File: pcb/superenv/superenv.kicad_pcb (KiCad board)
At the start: 2 copper layers, 100 x 100 mm, 25 parts, among them J1 TYPE-C-31-M-04, J2 Power-Header, J3 UART, J4 I2C, J5 I2C, U1 ESP32-C6-WROOM-1, U2 AMS1117-3.3, U3 DS18B20, U4 DS18B20, U5 DS18B20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

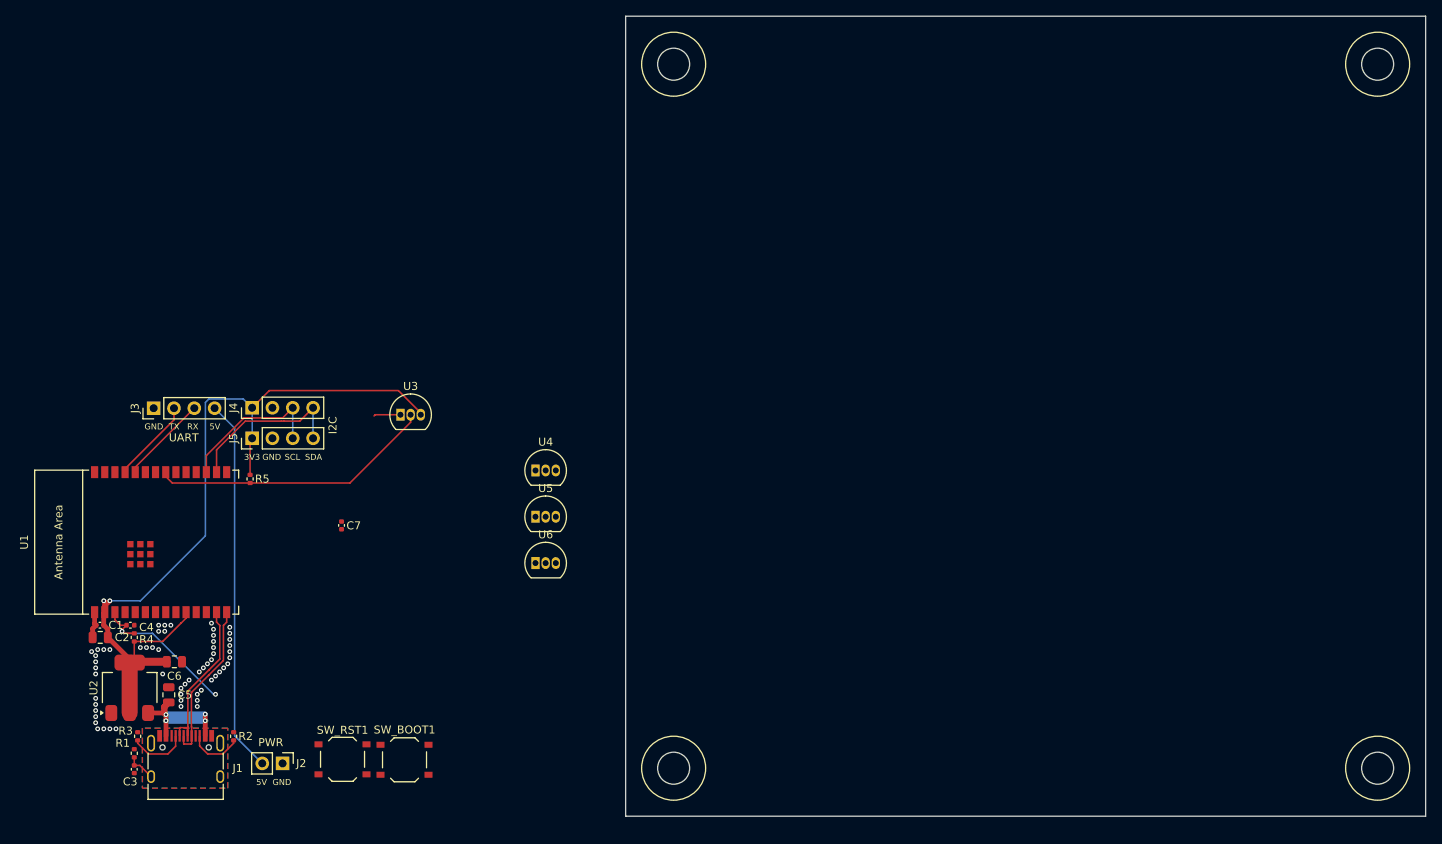
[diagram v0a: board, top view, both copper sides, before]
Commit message: Add I2C sensors
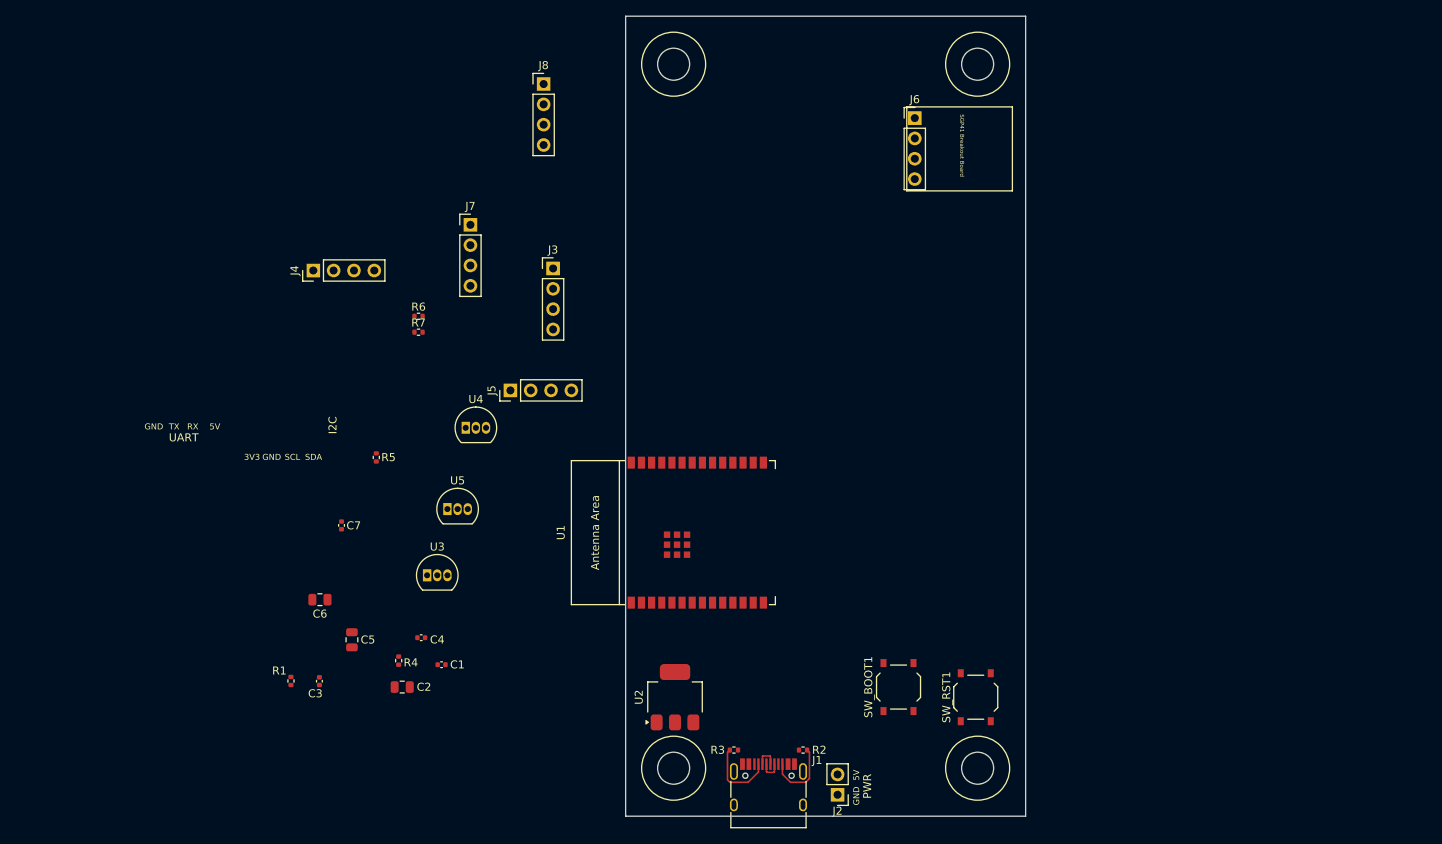
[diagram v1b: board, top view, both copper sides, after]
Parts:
- removed U6: DS18B20, Package_TO_SOT_THT:TO-92_Inline
- added J6: SGP41BB, Connector_PinHeader_2.54mm:PinHeader_1x04_P2.54mm_Vertical, F.Cu at (136.1, 62.7)
- added J7: SCD41BB, Connector_PinHeader_2.54mm:PinHeader_1x04_P2.54mm_Vertical, F.Cu at (80.6, 76.1)
- added J8: AHT20+BMP280BB, Connector_PinHeader_2.54mm:PinHeader_1x04_P2.54mm_Vertical, F.Cu at (89.8, 58.5)
- added R6: 4.7k, Resistor_SMD:R_0402_1005Metric, F.Cu at (74.1, 87.5)
- added R7: 4.7k, Resistor_SMD:R_0402_1005Metric, F.Cu at (74.1, 89.5)
- moved SW_RST1 79.5 mm to (143.8, 135.1), turned to -90 degrees
- moved R3 74.6 mm to (113.5, 141.7), turned to 0 degrees
- moved J1 72.9 mm to (117.9, 147.5)
- moved R2 71.2 mm to (122.2, 141.7), turned to 180 degrees
- moved J2 69.5 mm to (126.5, 147.3), turned to 180 degrees
- moved U2 68.2 mm to (106.2, 135.1)
- moved U1 67.1 mm to (109.0, 114.6)
- moved SW_BOOT1 62.4 mm to (134.1, 133.9), turned to 90 degrees
- moved J3 52.9 mm to (90.9, 81.5), turned to 0 degrees
- moved C1 43.0 mm to (77.0, 131.1)
- moved C2 38.3 mm to (72.1, 133.9)
- moved C4 36.4 mm to (74.5, 127.7)
- moved R4 33.2 mm to (71.6, 130.6)
- moved J5 32.8 mm to (85.6, 96.8)
- moved C3 25.6 mm to (61.7, 133.1)
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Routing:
- net +3V3: track 103.0 -> 0.00 mm, vias 2 -> 0
- net +5V: track 65.9 -> 0.00 mm, vias 4 -> 0
- net DQ: track 35.6 -> 0.00 mm
- net SDA: track 20.8 -> 0.00 mm
- net EN: track 20.3 -> 0.00 mm, vias 2 -> 0
- net SCL: track 19.2 -> 0.00 mm
- net USB_DN: track 20.3 -> 2.99 mm
- net USB_DP: track 20.3 -> 2.99 mm
- net RXD_0: track 11.1 -> 0.00 mm
- net TXD_0: track 10.5 -> 0.00 mm
- net GND: track 6.78 -> 0.00 mm, vias 58 -> 0
- net Net-(J1-SHIELD): track 3.69 -> 0.00 mm
- net Net-(J1-CC2): track 6.84 -> 8.92 mm
- net Net-(J1-CC1): track 7.36 -> 9.36 mm
- removed copper zone on B.Cu, net Net-(J1-SHIELD)
- removed copper zone on F.Cu, net Net-(J1-SHIELD)
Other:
- board size 100 x 100 mm -> 50 x 100 mm
- board text added: "SGP41 Breakout Board"

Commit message: Add stuff
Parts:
- added J10: PMSBB, Connector_JST:JST_GH_BM08B-GHS-TBT_1x08-1MP_P1.25mm_Vertical, F.Cu at (145.5, 108.1)
- added J9: UART1, Connector_PinHeader_2.54mm:PinHeader_1x04_P2.54mm_Vertical, F.Cu at (130.8, 118.9)
- J3: value UART -> UART0
- moved J7 77.6 mm to (145.8, 118.1), turned to -90 degrees
- moved J4 66.5 mm to (123.2, 105.2)
- moved R7 65.3 mm to (135.4, 112.0), turned to 90 degrees
- moved R6 64.3 mm to (133.6, 112.0), turned to 90 degrees
- moved C7 57.0 mm to (120.7, 123.5)
- moved R1 55.8 mm to (112.0, 147.6)
- moved J3 51.8 mm to (130.8, 114.6), turned to -90 degrees
- moved C3 51.3 mm to (111.0, 147.5), turned to -90 degrees
- moved C5 46.6 mm to (111.0, 139.1), turned to -90 degrees
- moved C6 45.7 mm to (107.0, 129.3)
- moved R5 41.7 mm to (110.5, 102.9), turned to 180 degrees
- moved J5 39.7 mm to (123.2, 109.5)
- moved R4 34.4 mm to (105.9, 127.3)
- moved C4 32.0 mm to (106.4, 125.2)
- moved C2 30.7 mm to (102.0, 127.0)
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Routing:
- net +3V3: track 0.00 -> 108.6 mm, vias 0 -> 1
- net +5V: track 0.00 -> 59.4 mm, vias 0 -> 4
- net SCL: track 0.00 -> 57.7 mm
- net SDA: track 0.00 -> 49.5 mm
- net BOOT: track 0.00 -> 38.0 mm, vias 0 -> 2
- net TXD_1: track 0.00 -> 30.6 mm
- net EN: track 0.00 -> 29.8 mm, vias 0 -> 2
- net TXD_0: track 0.00 -> 29.4 mm
- net RXD_1: track 0.00 -> 29.3 mm
- net RXD_0: track 0.00 -> 25.6 mm
- net USB_DP: track 2.99 -> 24.7 mm
- net USB_DN: track 2.99 -> 24.7 mm
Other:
- board text added: "SCD41 Breakout Board"

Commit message: Update gitignore and finish v1
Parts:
- removed the C3 at (111.0, 147.5)
- removed U5: DS18B20, Package_TO_SOT_THT:TO-92_Inline
- added C4: 100n, Capacitor_SMD:C_0603_1608Metric, F.Cu at (121.9, 123.4)
- added G***: LOGO, LOGO, B.Cu at (142.4, 119.5)
- added J11: DS18B20, Connector_PinHeader_2.54mm:PinHeader_1x03_P2.54mm_Vertical, F.Cu at (130.0, 139.2)
- added J12: GPIO, Connector_PinHeader_2.54mm:PinHeader_1x08_P2.54mm_Vertical, F.Cu at (110.0, 83.3)
- added J13: 3V3 rail, Connector_PinHeader_2.54mm:PinHeader_1x04_P2.54mm_Vertical, F.Cu at (101.9, 93.5)
- added J14: GND rail, Connector_PinHeader_2.54mm:PinHeader_1x04_P2.54mm_Vertical, F.Cu at (105.5, 93.5)
- added R8: 10k, Resistor_SMD:R_0603_1608Metric, F.Cu at (135.8, 131.6)
- added R9: 10k, Resistor_SMD:R_0603_1608Metric, F.Cu at (135.7, 130.0)
- C1: footprint Capacitor_SMD:C_0402_1005Metric -> Capacitor_SMD:C_0603_1608Metric
- C3: renamed from C4; footprint Capacitor_SMD:C_0402_1005Metric -> Capacitor_SMD:C_0603_1608Metric
- C7: value 100n -> 4.7n; footprint Capacitor_SMD:C_0402_1005Metric -> Capacitor_SMD:C_0603_1608Metric
- R1, R2, R3, R4, R5, R6, R7: footprint Resistor_SMD:R_0402_1005Metric -> Resistor_SMD:R_0603_1608Metric
- moved J8 54.4 mm to (134.5, 89.4)
- moved U3 54.1 mm to (130.0, 126.2), turned to -90 degrees
- moved U4 33.9 mm to (113.5, 96.3)
- moved J10 32.8 mm to (136.6, 139.7)
- moved C7 26.8 mm to (109.0, 147.6)
- moved J7 14.5 mm to (145.0, 103.6)
- moved J6 9.01 mm to (130.1, 96.8), turned to 180 degrees
- moved R5 7.54 mm to (117.9, 101.6)
- moved R3 2.99 mm to (111.0, 143.3), turned to 90 degrees
- moved R2 2.82 mm to (124.5, 143.3), turned to 90 degrees
- moved R7 1.65 mm to (136.1, 110.6), turned to -90 degrees
- moved R6 1.55 mm to (134.1, 110.6), turned to -90 degrees
- moved J2 1.26 mm to (127.5, 147.3)
- moved R1 1.02 mm to (111.0, 147.5)
- moved C3 0.60 mm to (106.9, 125.0)
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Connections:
- C7 pad 1: BOOT -> Net-(J1-SHIELD)
- J10 pad 1: unconnected-(J10-Pin_1-Pad1) -> +5V
- J10 pad 2: unconnected-(J10-Pin_2-Pad2) -> GND
- J10 pad 3: unconnected-(J10-Pin_3-Pad3) -> SET
- J10 pad 4: unconnected-(J10-Pin_4-Pad4) -> TXD_0
- J10 pad 5: unconnected-(J10-Pin_5-Pad5) -> RXD_0
- J10 pad 6: unconnected-(J10-Pin_6-Pad6) -> RST
- R6 pad 1: +3V3 -> SCL
- R6 pad 2: SCL -> +3V3
- R7 pad 1: +3V3 -> SDA
- R7 pad 2: SDA -> +3V3
- U1 pad 11: unconnected-(U1-GPIO10-Pad11) -> SET
- U1 pad 12: unconnected-(U1-GPIO11-Pad12) -> RST
- U1 pad 18: unconnected-(U1-GPIO20-Pad18) -> GPIO20
- U1 pad 19: unconnected-(U1-GPIO21-Pad19) -> GPIO21
- U1 pad 20: unconnected-(U1-GPIO22-Pad20) -> GPIO22
- U1 pad 4: unconnected-(U1-MTMS/GPIO4/ADC1_CH4-Pad4) -> GPIO4
- U1 pad 5: unconnected-(U1-MTDI/GPIO5/ADC1_CH5-Pad5) -> GPIO5
- U1 pad 6: unconnected-(U1-MTCK/GPIO6/ADC1_CH6-Pad6) -> GPIO6
- U1 pad 7: unconnected-(U1-MTDO/GPIO7-Pad7) -> GPIO7
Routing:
- net +3V3: track 108.6 -> 210.7 mm
- net DQ: track 0.00 -> 65.4 mm, vias 0 -> 1
- net RST: track 0.00 -> 48.4 mm, vias 0 -> 2
- net SET: track 0.00 -> 42.5 mm, vias 0 -> 2
- net GPIO4: track 0.00 -> 38.8 mm, vias 0 -> 1
- net GPIO5: track 0.00 -> 35.7 mm, vias 0 -> 1
- net GPIO6: track 0.00 -> 32.7 mm, vias 0 -> 1
- net RXD_0: track 25.6 -> 56.8 mm, vias 0 -> 1
- net GPIO7: track 0.00 -> 29.6 mm, vias 0 -> 1
- net TXD_0: track 29.4 -> 57.4 mm, vias 0 -> 1
- net +5V: track 59.4 -> 81.5 mm
- net GPIO20: track 0.00 -> 10.6 mm
- net GPIO21: track 0.00 -> 7.54 mm
- net GPIO22: track 0.00 -> 4.48 mm
- net SDA: track 49.5 -> 53.3 mm
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- added copper zone on B.Cu, net GND
- added copper zone on F.Cu, net GND
- added copper zone on B.Cu, net Net-(J1-SHIELD)
- added copper zone on F.Cu, net Net-(J1-SHIELD)
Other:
- board size 50 x 100 mm -> 50 x 70 mm
- board text added: "AHT21 + BMP280 Breakout Board"
- board text added: "Designed By Marcin Czop"
- board text added: "GP20"
- board text added: "GP21"
- board text added: "GP22"
- board text added: "GP4"
- board text added: "GP5"
- board text added: "GP6"
- board text added: "GP7"
